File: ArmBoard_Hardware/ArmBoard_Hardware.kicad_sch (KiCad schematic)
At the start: 61 parts, among them J1 RJ45_LED_Shielded, Q1 AO3401A, SW1 SW_Push, SW10 SW_Push, SW11 SW_Push, SW12 SW_SPDT, SW2 SW_Push, SW3 SW_Push, SW4 SW_Push, SW5 SW_Push, SW6 SW_Push, SW7 SW_Push, SW8 SW_Push, SW9 SW_Push, U1 PCF8574, U2 VNH7070AS, U3 OKI, U4 OKI, U5 Teensy4.1_DEV-16771

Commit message: Added tedious symbols
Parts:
- removed Conn14: Molex_SL_05, symbol MRDT_Connectors:Molex_SL_05
- removed Conn4, Conn5, Conn6: Molex_SL_04, symbol MRDT_Connectors:Molex_SL_04
- removed D10, D11, D12, D13, D14, D15, D16, D17, D18, D19, D20, D5, D6, D7, D8, D9: LED, symbol Device:LED
- removed SW11: SW_Push, symbol Switch:SW_Push
- removed U2: VNH7070AS, Package_SO:SOIC-14-16_3.9x9.9mm_P1.27mm, symbol MRDT_Devices:VNH7070AS
- removed U4: OKI, symbol MRDT_Devices:OKI
- added C4, C5: 10uF, symbol Device:C
- added C6: 10nF, symbol Device:C
- added C7: 100nF, symbol Device:C
- added Conn14, Conn28, Conn4, Conn5, Conn6: Molex_SL_02, symbol MRDT_Connectors:Molex_SL_02
- added Conn18, Conn19, Conn20, Conn21: Molex_SL_05, symbol MRDT_Connectors:Molex_SL_05
- added Conn22, Conn23, Conn24, Conn25, Conn26, Conn27: Molex_SL_04, symbol MRDT_Connectors:Molex_SL_04
- added R10, R11, R12, R13, R4, R5, R6, R7, R8, R9: R, symbol Device:R
- added R3: 620, symbol Device:R
- added U2: OKI, symbol MRDT_Devices:OKI
- added U4: ATA6561, Package_SO:SOIC-8_3.9x4.9mm_P1.27mm, symbol MRDT_Devices:ATA6561
- added V1, V2, V3, V4: Via, MRDT_Drill_Holes:4_40_Hole, symbol MRDT_Drill_Holes:Via
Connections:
- net +12V: now also C4.1, U2.1 (Vi)
- net +3V3: now also SW12.3 (C), C7.2, R10.1, R11.1, R12.1, R13.1, R4.1, R5.1, R6.1, R7.1, R8.1, R9.1, U4.5 (VIO)
- net GND: now also Conn10.2, Conn11.2, Conn12.2, Conn3.1, Conn7.2, Conn8.2, Conn9.2, D3.1 (K), SW1.1, SW10.1, SW12.1 (A), SW2.1, SW3.1, SW4.1, SW5.1, SW6.1, SW7.1, SW8.1, SW9.1, U5.GND1 (GND), U5.GND2 (GND), U5.GND3 (GND), U5.GND4 (GND), U5.GND5 (GND), U5.USB_GND1 (USB_GND), U5.USB_GND2 (USB_GND), C4.2, C5.2, C6.2, C7.1, Conn14.2, Conn22.1, Conn23.1, Conn24.1, Conn25.1, Conn26.1, Conn27.1, Conn4.2, Conn5.2, Conn6.2, U2.2 (GND), U4.2 (GND)
- net LED: now also U5.LED
- net Rx+: now also U5.R-
- net Rx-: now also U5.R+
- net Tx+: now also U5.T+
- net Tx-: now also U5.T-
- net LS_6: now reaches Conn7.1
- net at D3.2 (A): now also R3.2
- net DIR_SW: now reaches SW12.2 (B)
- net B_1: now reaches SW1.2
- net B_1: now also R4.2
- net SEL_2: now reaches Conn16.1
- net CS_2: now reaches Conn16.2
- net FWD_2: now reaches Conn16.3
- net RVS_2: now reaches Conn16.4
- net PWM_2: now reaches Conn16.5
- net B_4: now reaches SW4.2
- net B_4: now also R7.2
- net LS_2: now reaches Conn10.1
- net +5V: now reaches U5.VIN
- net +5V: now also Conn3.2, C5.1, C6.1, Conn22.2, Conn23.2, Conn24.2, Conn25.2, Conn26.2, Conn27.2, R3.1, U2.3 (Vo), U4.3 (VCC)
- net B_2: now reaches SW2.2
- net B_2: now also R5.2
- net B_SOL: now reaches SW10.2
- net B_SOL: now also R13.2
- net B_8: now reaches SW8.2
- net B_8: now also R11.2
- net LS_4: now reaches Conn12.1
- net LS_3: now reaches Conn11.1
- net B_5: now reaches SW5.2
- net B_5: now also R8.2
- net B_6: now reaches SW6.2
- net B_6: now also R9.2
- net B_3: now reaches SW3.2
- net B_3: now also R6.2
- net LS_1: now reaches Conn9.1
- net SEL_6: now reaches Conn17.1
- net CS_6: now reaches Conn17.2
- net FWD_6: now reaches Conn17.3
- net RVS_6: now reaches Conn17.4
- net PWM_6: now reaches Conn17.5
- net SEL_1: now reaches Conn13.1
- net CS_1: now reaches Conn13.2
- net FWD_1: now reaches Conn13.3
- net RVS_1: now reaches Conn13.4
- net PWM_1: now reaches Conn13.5
- net LS_10: now reaches Conn8.1
- net B_LAS: now reaches SW9.2
- net B_LAS: now also R12.2
- net SEL_5: now reaches Conn15.1
- net CS_5: now reaches Conn15.2
- net FWD_5: now reaches Conn15.3
- net RVS_5: now reaches Conn15.4
- net PWM_5: now reaches Conn15.5
- net EncoderA_1: now reaches Conn3.3
- net EncoderB_1: now reaches Conn3.4
- net B_7: now reaches SW7.2
- net B_7: now also R10.2
- new net CANH: U4.7 (CANH)
- new net CANL: U4.6 (CANL)
- new net CS_3: Conn18.2
- new net CS_4: Conn20.2
- new net CS_7: Conn19.2
- new net CS_8: Conn21.2
- new net EncoderA_2: Conn23.3
- new net EncoderA_3: Conn25.3
- new net EncoderA_4: Conn27.3
- new net EncoderA_5: Conn22.3
- new net EncoderA_6: Conn24.3
- new net EncoderA_7: Conn26.3
- new net EncoderB_2: Conn23.4
- new net EncoderB_3: Conn25.4
- new net EncoderB_4: Conn27.4
- new net EncoderB_5: Conn22.4
- new net EncoderB_6: Conn24.4
- new net EncoderB_7: Conn26.4
- new net FWD_3: Conn18.3
- new net FWD_4: Conn20.3
- new net FWD_7: Conn19.3
- new net FWD_8: Conn21.3
- new net LS_5: Conn14.1
- new net LS_7: Conn4.1
- new net LS_8: Conn5.1
- new net LS_9: Conn6.1
- new net PWM_3: Conn18.5
- new net PWM_4: Conn20.5
- new net PWM_7: Conn19.5
- new net PWM_8: Conn21.5
- new net RVS_3: Conn18.4
- new net RVS_4: Conn20.4
- new net RVS_7: Conn19.4
- new net RVS_8: Conn21.4
- new net SEL_3: Conn18.1
- new net SEL_4: Conn20.1
- new net SEL_7: Conn19.1
- new net SEL_8: Conn21.1
- no-connect marks 3 -> 7
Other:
- moved on the sheet: C1, C2, C3, Conn13, Conn1A, Conn1B, Conn2A, Conn2B, Conn3, Conn7, D1, D2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

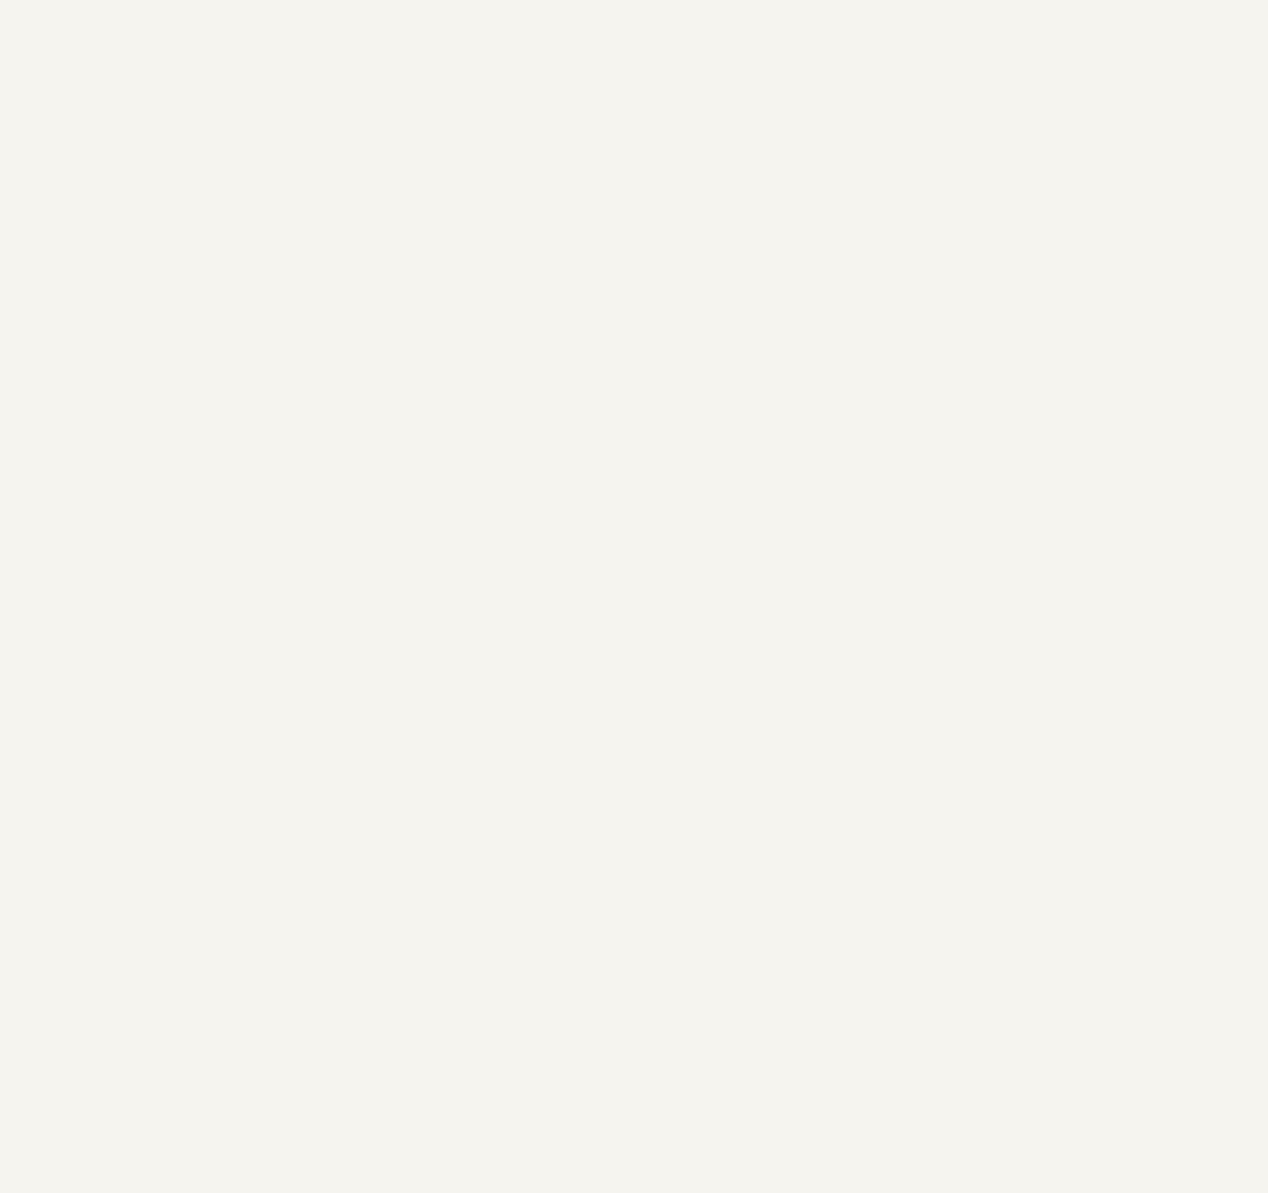
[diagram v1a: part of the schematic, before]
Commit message: Encoder/Decoders
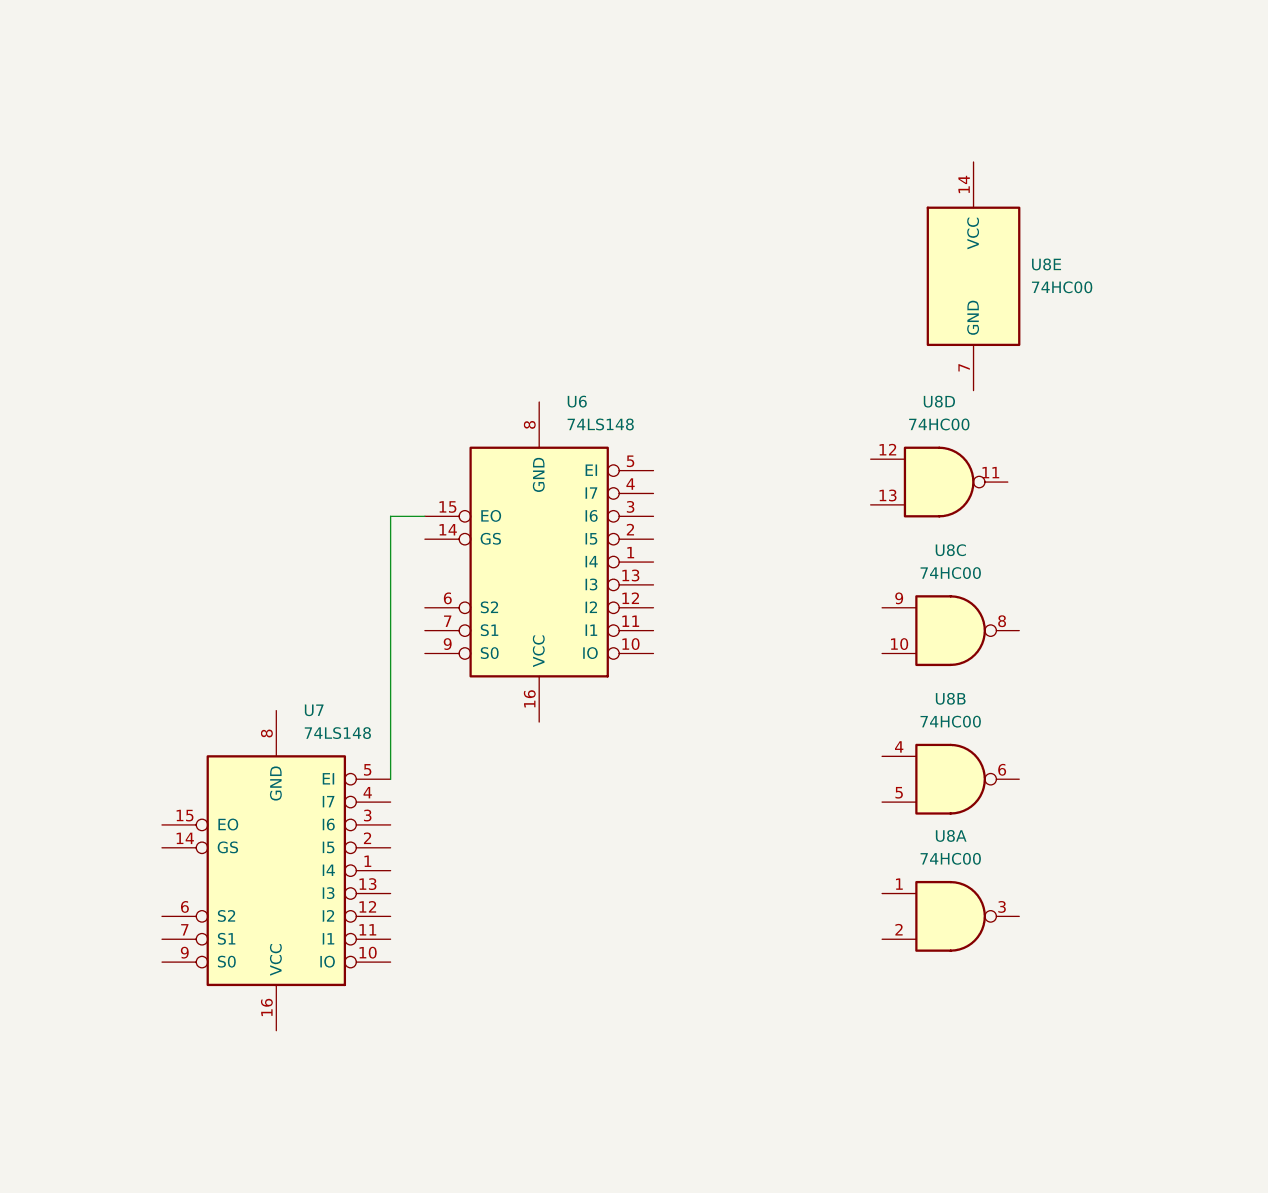
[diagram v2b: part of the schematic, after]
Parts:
- added U6, U7: 74LS148, symbol 74xx:74LS148
- added U8: 74HC00, symbol 74xx:74HC00
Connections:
- new net: U6.15 (EO), U7.5 (EI)

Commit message: Added teensy labels
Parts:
- removed Conn22, Conn24, Conn25, Conn26, Conn27: Molex_SL_04, symbol MRDT_Connectors:Molex_SL_04
- added C8: 4.7nF, symbol Device:C
- added Conn22, Conn25, Conn26, Conn27: Molex_SL_03, symbol MRDT_Connectors:Molex_SL_03
- added R14, R15: 60, symbol Device:R
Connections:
- net CANH is gone; now on an unnamed net: U4.7 (CANH)
- net CANL is gone; now on an unnamed net: U4.6 (CANL)
- net SEL_1 is gone; now on net +3V3: Conn13.1
- net SEL_2 is gone; now on net +3V3: Conn16.1
- net SEL_3 is gone; now on net +3V3: Conn18.1
- net SEL_4 is gone; now on net +3V3: Conn20.1
- net SEL_5 is gone; now on net +3V3: Conn15.1
- net SEL_6 is gone; now on net +3V3: Conn17.1
- net SEL_7 is gone; now on net +3V3: Conn19.1
- net SEL_8 is gone; now on net +3V3: Conn21.1
- net +5V: now also Conn23.1, Conn3.1, Conn22.1, Conn25.1, Conn26.1, Conn27.1; no longer Conn23.2, Conn3.2
- net CS_1: now also U5.14 (A0)
- net CS_2: now also U5.15 (A1)
- net CS_3: now also U5.16 (A2)
- net CS_4: now also U5.17 (A3)
- net CS_5: now also U5.23 (A9)
- net CS_6: now also U5.20 (A6)
- net CS_7: now also U5.21 (A7)
- net CS_8: now also U5.22 (A8)
- net EncoderA_1: now also Conn3.2, U5.41 (A17); no longer Conn3.3
- net EncoderA_2: now also Conn23.2, U5.39 (A15); no longer Conn23.3
- net EncoderB_1: now also Conn3.3, U5.40 (A16); no longer Conn3.4
- net EncoderB_2: now also Conn23.3, U5.38 (A14); no longer Conn23.4
- net GND: now also Conn23.4, Conn3.4, C8.2, Conn22.3, Conn25.3, Conn26.3, Conn27.3; no longer Conn23.1, Conn3.1
- net PWM_1: now also U5.2 (OUT2)
- net PWM_2: now also U5.3 (LRCLK2)
- net PWM_3: now also U5.4 (BCLK2)
- net PWM_4: now also U5.5 (IN2)
- net PWM_5: now also U5.6 (OUT1D)
- net PWM_6: now also U5.7 (RX2)
- net PWM_7: now also U5.8 (TX2)
- net PWM_8: now also U5.9 (OUT1C)
- net at Conn28.1: now also R14.1
- net at Conn28.2: now also R15.2
- net CANRX: now reaches U5.0 (RX1)
- net CANRX: now also U4.4 (RXD)
- net CANTX: now reaches U5.1 (TX1)
- net CANTX: now also U4.1 (TXD)
- net SDA: now reaches U5.18 (A4)
- net SCL: now reaches U5.19 (A5)
- net ABS_4: now reaches U5.24 (A10)
- net ABS_4: now also Conn27.2
- net ABS_3: now reaches U5.25 (A11)
- net ABS_3: now also Conn26.2
- net ABS_2: now reaches U5.26 (A12)
- net ABS_2: now also Conn25.2
- net ABS_1: now reaches U5.27 (A13)
- net ABS_1: now also Conn22.2
- net BENC_1: now reaches U5.28 (RX7)
- net BENC_2: now reaches U5.29 (TX7)
- net STBY: now reaches U5.31 (CTX3)
- net STBY: now also U4.8 (STBY)
- net LAS: now reaches U5.33 (MCLK2)
- net BENC_3: now reaches U5.34 (RX8)
- net BENC_4: now reaches U5.35 (TX8)
- new net: C8.1, R14.2, R15.1
- no-connect marks 7 -> 11
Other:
- moved on the sheet: Conn28, U1, U8D

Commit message: Finished schematic before review
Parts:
- removed Conn21: Molex_SL_05, symbol MRDT_Connectors:Molex_SL_05
- removed Q1: AO3401A, Package_TO_SOT_SMD:SOT-23, symbol Transistor_FET:AO3401A
- removed U6: 74LS148, symbol 74xx:74LS148
- removed U8: 74HC00, symbol 74xx:74HC00
- added Conn21, Conn24: Molex_SL_02, MRDT_Connectors:MOLEX_SL_02_Vertical, symbol MRDT_Connectors:Molex_SL_02
- added Conn29: Molex_SL_05, symbol MRDT_Connectors:Molex_SL_05
- added D10, D11, D12, D13, D7, D8, D9: Blue, symbol Device:LED
- added D5, D6: Orange, LED_SMD:LED_0603_1608Metric_Pad1.05x0.95mm_HandSolder, symbol Device:LED
- added Q1, Q10, Q11, Q5, Q6, Q7, Q8, Q9: T2N7002AK,LM, Package_TO_SOT_SMD:SOT-23-3, symbol T2N7002AK_LM:T2N7002AK,LM
- added Q2, Q3: BSS138, Package_TO_SOT_SMD:SOT-23, symbol Transistor_FET:BSS138
- added Q4: AO3401A, Package_TO_SOT_SMD:SOT-23, symbol Transistor_FET:AO3401A
- added R16, R17, R18, R19, R20, R21, R22, R23, R24, R25, R26, R27: 4.7k, symbol Device:R
- added R28, R30: 4.7k, Resistor_SMD:R_0603_1608Metric_Pad0.98x0.95mm_HandSolder, symbol Device:R
- added R29: 620, Resistor_SMD:R_0603_1608Metric_Pad0.98x0.95mm_HandSolder, symbol Device:R
- added R31, R32: 10k, Resistor_SMD:R_0603_1608Metric_Pad0.98x0.95mm_HandSolder, symbol Device:R
- added R33: 2.2k, Resistor_SMD:R_0603_1608Metric_Pad0.98x0.95mm_HandSolder, symbol Device:R
- added R34, R35, R36, R37, R38, R39, R40, R41: 220, symbol Device:R
- added U10, U9: PCF8574, symbol Interface_Expansion:PCF8574
- added U6: 74HC00, Package_SO:SO-14_3.9x8.65mm_P1.27mm, symbol 74xx:74HC00
- added U8: 74LS148, Package_SO:SOIC-16_3.9x9.9mm_P1.27mm, symbol 74xx:74LS148
- Conn1: footprint (none) -> MRDT_Connectors:Square_Anderson_2_H_Side_By_Side
- D4: value LED -> Blue
- U7: footprint (none) -> Package_SO:SOIC-16_3.9x9.9mm_P1.27mm
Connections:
- net BENC_4 is gone; now on net BENC_3: U5.35 (TX8)
- net +12V: now also Q4.2 (S), R31.1
- net +3V3: now also C7.1, Conn10.1, Conn11.1, Conn12.1, Conn14.1, Conn4.1, Conn5.1, Conn6.1, Conn7.1, Conn8.1, Conn9.1, U1.16 (VDD), U7.16 (VCC), Conn29.1, R16.1, R17.1, R34.1, R35.1, R36.1, R37.1, R38.1, R39.1, R40.1, R41.1, U10.16 (VDD), U10.2 (A1), U6.14 (VCC), U8.1 (I4), U8.12 (I2), U8.13 (I3), U8.16 (VCC), U8.2 (I5), U8.3 (I6), U8.4 (I7), U9.1 (A0), U9.16 (VDD); no longer C7.2
- net +5V: now also Conn21.1, Conn24.1, D5.2 (A)
- net BENC_1: now also U5.29 (TX7), U6.6; no longer U5.28 (RX7)
- net BENC_2: now also U5.34 (RX8), U6.8; no longer U5.29 (TX7)
- net BENC_3: now also U7.5 (EI), U8.15 (EO); no longer U5.34 (RX8)
- net B_1: now also U7.10 (IO)
- net B_2: now also U7.11 (I1)
- net B_3: now also U7.12 (I2)
- net B_4: now also U7.13 (I3)
- net B_5: now also U7.1 (I4)
- net B_6: now also U7.2 (I5)
- net B_7: now also U7.3 (I6)
- net B_8: now also U7.4 (I7)
- net B_LAS: now also U8.10 (IO)
- net B_SOL: now also U8.11 (I1)
- net CS_8: now also Conn29.2
- net DIR_SW: now also U5.33 (MCLK2)
- net FWD_1: now also U9.6 (P2)
- net FWD_2: now also U9.9 (P4)
- net FWD_3: now also U9.11 (P6)
- net FWD_4: now also U10.4 (P0)
- net FWD_5: now also U10.6 (P2)
- net FWD_6: now also U10.9 (P4)
- net FWD_7: now also U10.11 (P6)
- net FWD_8: now also U5.11 (MOSI), Conn29.3
- net GND: now also C7.2, Conn1.1 (GND), U1.1 (A0), U1.2 (A1), U1.3 (A2), U1.8 (VSS), U7.8 (GND), D6.1 (K), Q1.2 (S), Q10.2 (S), Q11.2 (S), Q2.2 (S), Q3.2 (S), Q5.2 (S), Q6.2 (S), Q7.2 (S), Q8.2 (S), Q9.2 (S), R18.2, R19.2, R20.2, R21.2, R22.2, R23.2, R24.2, R25.2, R26.2, R27.2, R28.2, R30.2, U10.1 (A0), U10.3 (A2), U10.8 (VSS), U6.7 (GND), U8.5 (EI), U8.8 (GND), U9.2 (A1), U9.3 (A2), U9.8 (VSS); no longer C7.1, Conn10.2, Conn11.2, Conn12.2, Conn14.2, Conn4.2, Conn5.2, Conn6.2, Conn7.2, Conn8.2, Conn9.2
- net LAS: now also U5.13 (SCK), Q2.1 (G), R28.1; no longer U5.33 (MCLK2)
- net LS_1: now also Conn9.2, U1.4 (P0), R25.1; no longer Conn9.1
- net LS_10: now also Conn14.2, R26.1, U9.5 (P1); no longer Conn8.1
- net LS_2: now also Conn5.2, U1.5 (P1), R24.1; no longer Conn10.1
- net LS_3: now also Conn7.2, U1.6 (P2), R23.1; no longer Conn11.1
- net LS_4: now also Conn10.2, U1.7 (P3), R22.1; no longer Conn12.1
- net LS_5: now also Conn12.2, U1.9 (P4), R21.1; no longer Conn14.1
- net LS_6: now also Conn4.2, U1.10 (P5), R20.1; no longer Conn7.1
- net LS_7: now also Conn6.2, U1.11 (P6), R19.1; no longer Conn4.1
- net LS_8: now also Conn8.2, U1.12 (P7), R18.1; no longer Conn5.1
- net LS_9: now also Conn11.2, R27.1, U9.4 (P0); no longer Conn6.1
- net PWM_1: now also Q5.1 (G)
- net PWM_2: now also Q1.1 (G)
- net PWM_3: now also Q6.1 (G)
- net PWM_4: now also Q7.1 (G)
- net PWM_5: now also Q8.1 (G)
- net PWM_6: now also Q9.1 (G)
- net PWM_7: now also Q10.1 (G)
- net PWM_8: now also U5.36 (CS2), Conn29.5, Q11.1 (G); no longer U5.9 (OUT1C)
- net RVS_1: now also U9.7 (P3)
- net RVS_2: now also U9.10 (P5)
- net RVS_3: now also U9.12 (P7)
- net RVS_4: now also U10.5 (P1)
- net RVS_5: now also U10.7 (P3)
- net RVS_6: now also U10.10 (P5)
- net RVS_7: now also U10.12 (P7)
- net RVS_8: now also U5.12 (MISO), Conn29.4
- net SCL: now also U1.14 (SCL), R16.2, U10.14 (SCL), U9.14 (SCL)
- net SDA: now also U1.15 (SDA), R17.2, U10.15 (SDA), U9.15 (SDA)
- net at U7.14 (GS): now also U6.13
- net at U7.6 (S2): now also U6.10
- net at U7.7 (S1): now also U6.5
- net at U7.9 (S0): now also U6.2
- net at D4.1 (K): now also Q5.3 (D)
- net at D4.2 (A): now also R34.2
- net Solenoid: now reaches U5.10 (CS1)
- net Solenoid: now also Q3.1 (G), R30.1
- net at Conn1.2 (V+Log): now also Q4.3 (D), R33.1
- new net: D10.1 (K), Q8.3 (D)
- new net: Conn21.2, Conn24.2, Q2.3 (D), R29.2
- new net: D13.1 (K), Q11.3 (D)
- new net: D5.1 (K), R29.1
- new net: Q4.1 (G), R31.2, R32.1
- new net: D12.1 (K), Q10.3 (D)
- new net: D7.1 (K), Q1.3 (D)
- new net: D7.2 (A), R35.2
- new net: D9.1 (K), Q7.3 (D)
- new net: D11.1 (K), Q9.3 (D)
- new net: D11.2 (A), R39.2
- new net: U6.4, U8.7 (S1)
- new net: D12.2 (A), R40.2
- new net: Q3.3 (D), R32.2
- new net: D9.2 (A), R37.2
- new net: D8.1 (K), Q6.3 (D)
- new net: D13.2 (A), R41.2
- new net: D10.2 (A), R38.2
- new net: D6.2 (A), R33.2
- new net: U6.12, U8.14 (GS)
- new net: D8.2 (A), R36.2
- new net: U6.9, U8.6 (S2)
- new net: U6.1, U8.9 (S0)
- new net BENC_0: U5.28 (RX7), U6.3
- no-connect marks 11 -> 16
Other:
- note added: "16:4 Encoder"
- note added: "Buttons and Switch"
- note added: "CAN Transceiver"
- note added: "Encoders"
- note added: "IO Expanders"
- note added: "LEDs"
- note added: "Laser and Solenoid"
- note added: "Limit Switches"
- note added: "MoCo Signals"
- note added: "Mounting Holes"
- note added: "Power"
- note added: "Teensy and Ethernet Port"
- moved on the sheet: C1, C2, C3, C4, C5, C6, C7, C8, Conn13, Conn15, Conn16, Conn17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

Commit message: Changes made
Deleted extra wire
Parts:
- added C9: 100uF, symbol Device:C_Polarized
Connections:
- net +12V: now also C9.1
- net +3V3: now also Conn13.5, Conn15.5, Conn16.5, Conn17.5, Conn18.5, Conn19.5, Conn20.5, Conn29.5; no longer Conn13.1, Conn15.1, Conn16.1, Conn17.1, Conn18.1, Conn19.1, Conn20.1, Conn29.1
- net CS_1: now also Conn13.3; no longer Conn13.2
- net CS_2: now also Conn15.3; no longer Conn16.2
- net CS_3: now also Conn16.3; no longer Conn18.2
- net CS_4: now also Conn17.3; no longer Conn20.2
- net CS_5: now also Conn18.3; no longer Conn15.2
- net CS_6: now also Conn19.3; no longer Conn17.2
- net CS_7: now also Conn20.3; no longer Conn19.2
- net CS_8: now also Conn29.3; no longer Conn29.2
- net FWD_1: now also Conn13.4; no longer Conn13.3
- net FWD_2: now also Conn15.4; no longer Conn16.3
- net FWD_3: now also Conn16.4; no longer Conn18.3
- net FWD_4: now also Conn17.4; no longer Conn20.3
- net FWD_5: now also Conn18.4; no longer Conn15.3
- net FWD_6: now also Conn19.4; no longer Conn17.3
- net FWD_7: now also Conn20.4; no longer Conn19.3
- net FWD_8: now also Conn29.4; no longer Conn29.3
- net GND: now also C9.2
- net PWM_1: now also Conn13.2; no longer Conn13.5
- net PWM_2: now also Conn15.2; no longer Conn16.5
- net PWM_3: now also Conn16.2; no longer Conn18.5
- net PWM_4: now also Conn17.2; no longer Conn20.5
- net PWM_5: now also Conn18.2; no longer Conn15.5
- net PWM_6: now also Conn19.2; no longer Conn17.5
- net PWM_7: now also Conn20.2; no longer Conn19.5
- net PWM_8: now also Conn29.2; no longer Conn29.5
- net RVS_1: now also Conn13.1; no longer Conn13.4
- net RVS_2: now also Conn15.1; no longer Conn16.4
- net RVS_3: now also Conn16.1; no longer Conn18.4
- net RVS_4: now also Conn17.1; no longer Conn20.4
- net RVS_5: now also Conn18.1; no longer Conn15.4
- net RVS_6: now also Conn19.1; no longer Conn17.4
- net RVS_7: now also Conn20.1; no longer Conn19.4
- net RVS_8: now also Conn29.1; no longer Conn29.4

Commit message: psuh
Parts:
- D1, D2, D3: value LED -> Green
- R1: value 2.2k -> 680
- R2: value 330 -> 100
- R3: value 620 -> 220
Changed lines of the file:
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@@
 			)
 		)
-		(property "Value" "2.2k"
+		(property "Value" "680"
 			(at 215.9 55.8799 0)
 			(effects
@@
 			)
 		)
-		(property "Value" "LED"
+		(property "Value" "Green"
 			(at 228.6 66.3574 90)
 			(effects
@@
 			)
 		)
-		(property "Value" "LED"
+		(property "Value" "Green"
 			(at 217.17 66.3574 90)
 			(effects
@@
 			)
 		)
-		(property "Value" "LED"
+		(property "Value" "Green"
 			(at 240.03 66.3574 90)
 			(effects
@@
 			)
 		)
-		(property "Value" "330"
+		(property "Value" "100"
 			(at 238.76 55.8799 0)
 			(effects
@@
 			)
 		)
-		(property "Value" "620"
+		(property "Value" "220"
 			(at 227.33 55.8799 0)
 			(effects
